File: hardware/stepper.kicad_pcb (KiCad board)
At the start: 4 copper layers, 40 x 40 mm, 128 parts, among them J101 USB-MINI-B-SMD, J102 DRILL, J103 DRILL, J104 DRILL, J105 DRILL, J401 STACK-UP-HIGH, J402 STACK-DOWN, J403 STACK-UP-HIGH, J404 STACK-DOWN, P201 black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

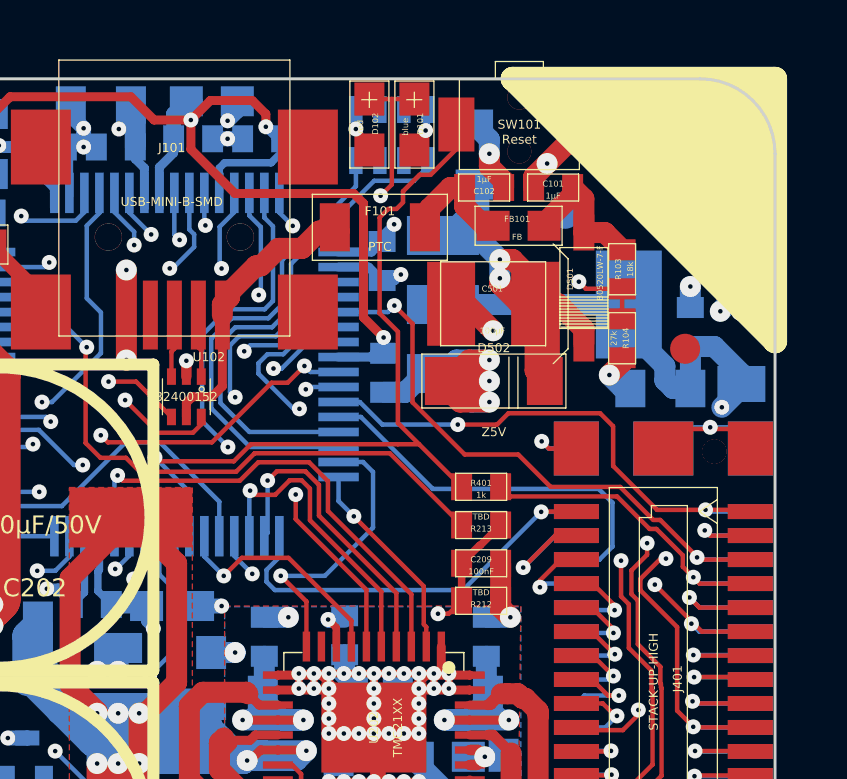
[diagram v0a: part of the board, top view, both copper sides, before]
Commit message: update to new library settings
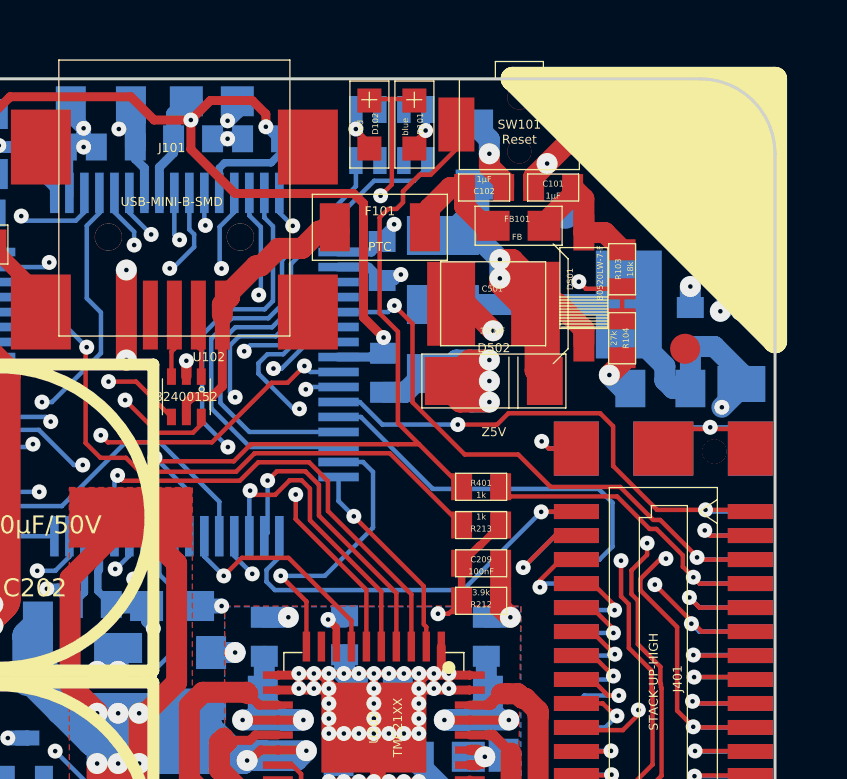
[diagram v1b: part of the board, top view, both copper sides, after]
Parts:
- C103, C104: value 9pF -> DNP
- D101, D102: footprint kicad-libraries:D0603E -> kicad-libraries:D0603
- R212: value TBD -> 3.9k
- R213: value TBD -> 1k
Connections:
- FILTER301 pad 8: (no net) -> Net-(FILTER301-Pad8)
- FILTER301 pad 9: (no net) -> Net-(FILTER301-Pad9)
- FILTER302 pad 8: (no net) -> Net-(FILTER302-Pad8)
- FILTER302 pad 9: (no net) -> Net-(FILTER302-Pad9)
- J101 pad 4: (no net) -> Net-(J101-Pad4)
- RP101 pad 2: (no net) -> Net-(RP101-Pad2)
- RP101 pad 3: (no net) -> Net-(RP101-Pad3)
- RP101 pad 6: (no net) -> Net-(RP101-Pad6)
- RP101 pad 7: (no net) -> Net-(RP101-Pad7)
- RP301 pad 6: (no net) -> Net-(RP301-Pad6)
- RP301 pad 7: (no net) -> Net-(RP301-Pad7)
- U101 pad 40: (no net) -> Net-(U101-Pad40)
- U101 pad 50: (no net) -> Net-(U101-Pad50)
- U202 pad 9: (no net) -> Net-(U202-Pad9)
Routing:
- net VSTACK: track 86.5 -> 88.1 mm
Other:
- board text added: "Copyright Tinkerforge GmbH 2016. This documentation describes Open Hardware and is licensed under the CERN OHL v. 1.1. You may redistribute and modify this documentation under the terms of the CERN OHL v.1.1. (http://ohwr.org/cernohl). This documentation is distributed WITHOUT ANY EXPRESS OR IMPLIED WARRANTY, INCLUDING OF MERCHANTABILITY, SATISFACTORY QUALITY AND FITNESS FOR A PARTICULAR PURPOSE.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"
- board text removed: "Copyright Tinkerforge GmbH 2015. This documentation describes Open Hardware and is licensed under the CERN OHL v. 1.1. You may redistribute and modify this documentation under the terms of the CERN OHL v.1.1. (http://ohwr.org/cernohl). This documentation is distributed WITHOUT ANY EXPRESS OR IMPLIED WARRANTY, INCLUDING OF MERCHANTABILITY, SATISFACTORY QUALITY AND FITNESS FOR A PARTICULAR PURPOSE.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"

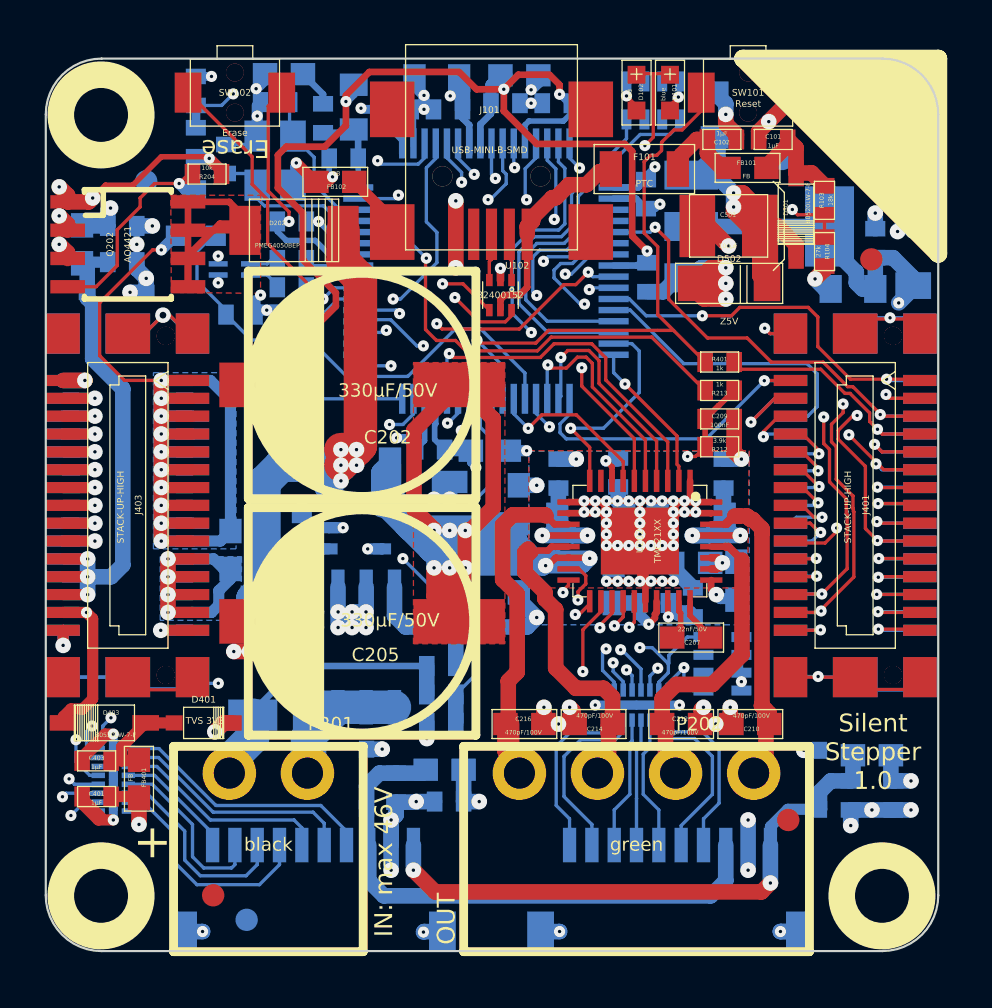
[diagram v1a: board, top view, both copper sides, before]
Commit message: fix tf logo, remove current measurement
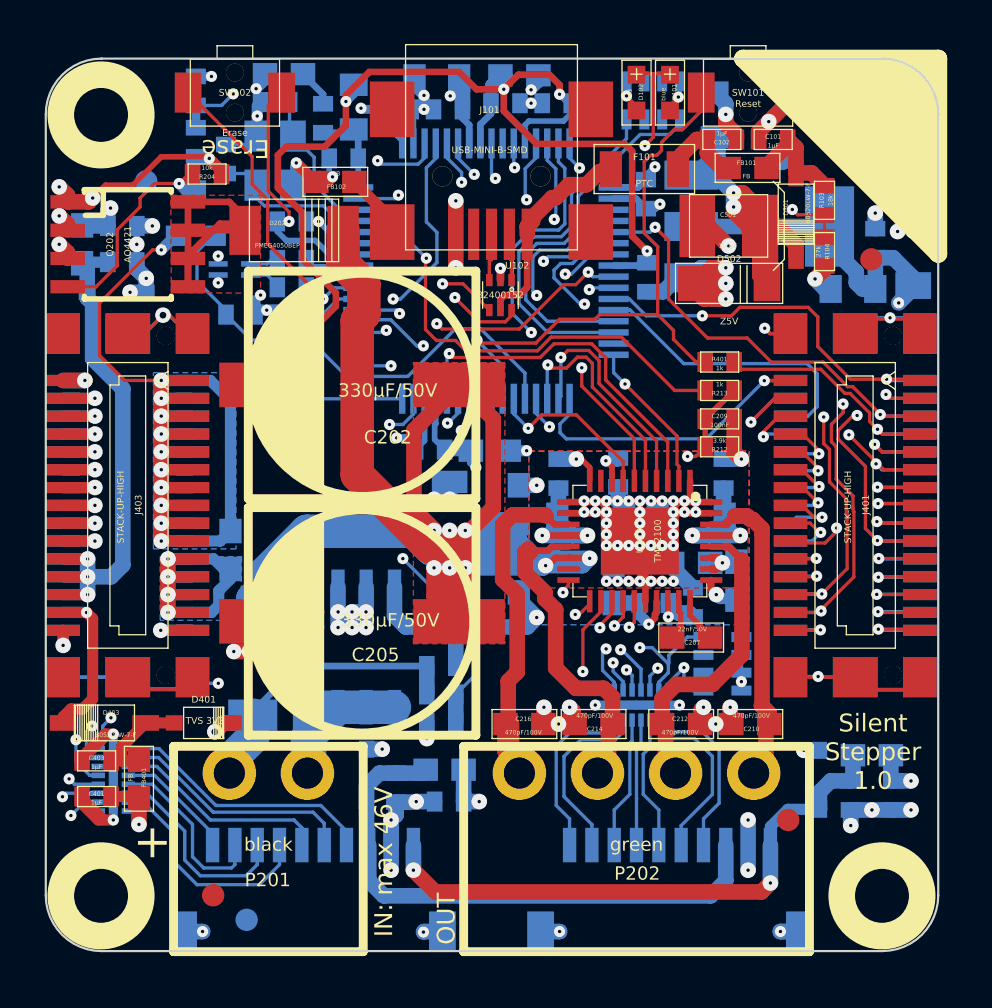
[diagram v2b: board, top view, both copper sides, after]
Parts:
- removed the G*** at (157.5, 85.2)
- removed R209: 0.01, kicad-libraries:1206
- removed R210: 10k, kicad-libraries:0402E
- removed U201: ZXCT1086, kicad-libraries:SOT23-5
- added G***: Logo_31x31, kicad-libraries:Logo_31x31, B.Cu at (157.5, 85.2)
- U202: value TMC21XX -> TMC2100
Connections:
- net PWR-CS_CFG3 renamed PWR-CFG3
- net PWR-DCEN_CFG4 renamed PWR-CFG4
- net PWR-DCIN_CFG5 renamed PWR-CFG5
- net PWR-SCK_CFG2 renamed PWR-CFG2
- net PWR-SD0_CFG0 renamed PWR-CFG0
- net PWR-SDI_CFG1 renamed PWR-CFG1
- D202 pad 2: Net-(D202-Pad2) -> VEE
- D203 pad 2: Net-(D202-Pad2) -> VEE
- U101 pad 10: PWR-CUR-SENSE -> Net-(U101-Pad10)
- U101 pad 31: PWR-SPI_MODE -> Net-(U101-Pad31)
- U101 pad 41: PWR-DC0 -> Net-(U101-Pad41)
- U202 pad 10: PWR-SPI_MODE -> STACK-PGND
- U202 pad 17: PWR-DC0 -> Net-(U202-Pad17)
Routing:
- net Net-(D202-Pad2): track 30.2 -> 0.00 mm, vias 5 -> 0
- net 3V3: track 192.1 -> 169.6 mm, vias 14 -> 13
- net PWR-CUR-SENSE: track 21.5 -> 0.00 mm, vias 2 -> 0
- net VEE: track 77.8 -> 95.8 mm
- net PWR-DC0: track 14.6 -> 0.00 mm, vias 2 -> 0
- net PWR-SPI_MODE: track 9.60 -> 0.00 mm, vias 1 -> 0
- net GND: track 435.4 -> 430.1 mm, vias 63 -> 62
- net STACK-PGND: track 217.1 -> 218.5 mm
- net Net-(R210-Pad2): track 1.28 -> 0.00 mm

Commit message: fix wrong bricklet select voltages
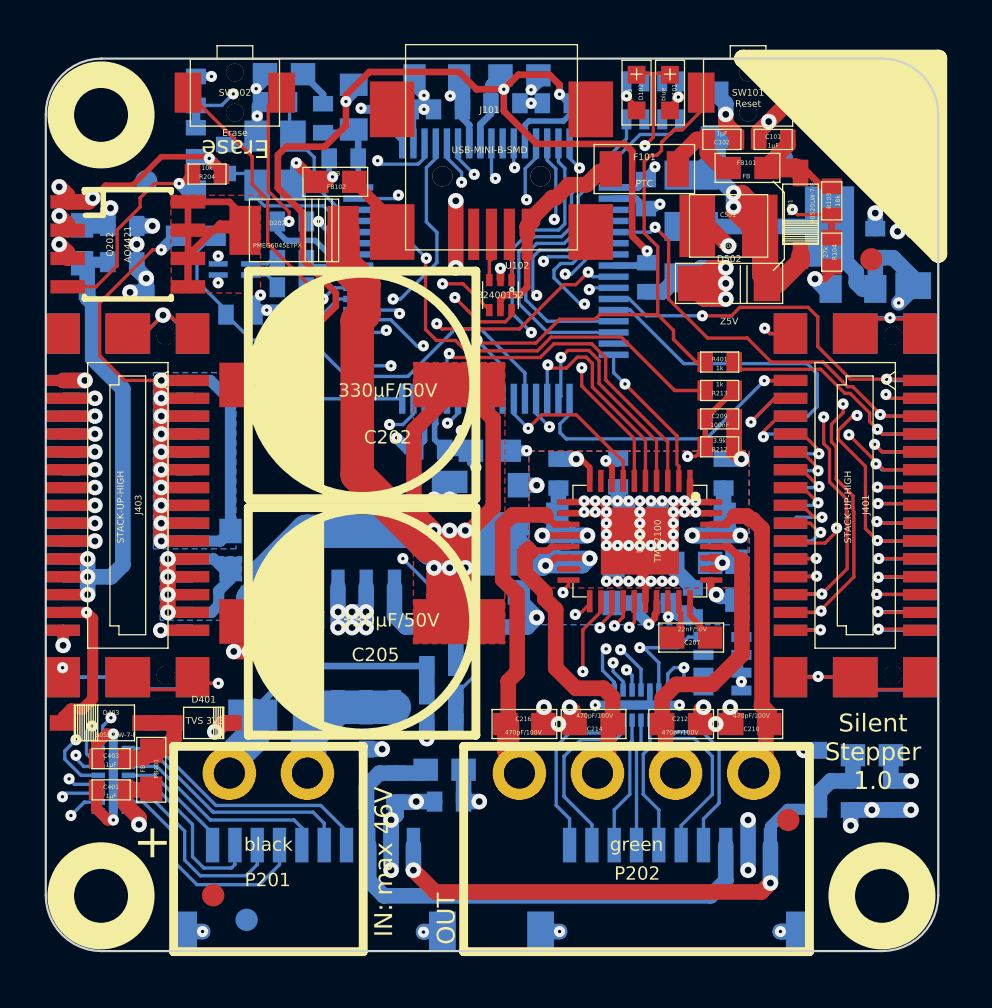
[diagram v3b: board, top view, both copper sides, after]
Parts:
- D202, D203: value PMEG4050BEP -> PMEG6045ETPX
- Q201: value FDS8449 -> AO4438
- moved C401 0.72 mm to (129.7, 105.5)
- moved FB401 0.68 mm to (131.4, 104.7)
- moved C403 0.66 mm to (129.7, 104.2)
- moved R103 0.33 mm to (161.9, 79.2)
- moved R104 0.33 mm to (161.9, 81.5)
- moved D501 0.20 mm to (160.6, 79.8)
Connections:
- FILTER301 pad 14: GND -> 3V3
- FILTER302 pad 14: 3V3 -> GND
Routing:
- net 3V3: track 169.6 -> 177.6 mm
- net GND: track 430.1 -> 428.7 mm, vias 62 -> 63
- net BRICKLET-IO0_3: track 39.4 -> 40.0 mm
- net BRICKLET-I2C-SCL: track 54.7 -> 55.3 mm

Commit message: detail routing improvements
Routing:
- net STACK-RESET: track 26.7 -> 28.3 mm
- net STACK-I2C-SDA/JTAG-TDI: track 14.4 -> 12.9 mm
- net STACK-I2C-SCL/JTAG-TDO: track 23.3 -> 24.4 mm
- net Net-(J401-Pad6): track 2.99 -> 3.74 mm
- net STACK-PGND: track 218.5 -> 219.2 mm
- net Net-(J401-Pad8): track 3.04 -> 3.73 mm
- net 3V3: track 177.6 -> 178.2 mm
- net Net-(SW102-Pad1): track 13.6 -> 14.1 mm
- net PWR-CFG5: track 24.6 -> 25.1 mm
- added copper zone on F.Cu, net STACK-PVCC

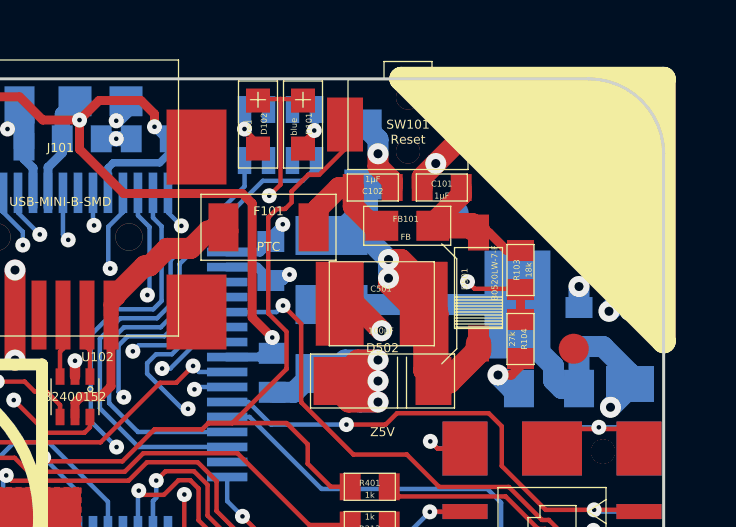
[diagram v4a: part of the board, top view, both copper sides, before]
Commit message: move leds from border, delete to near doku
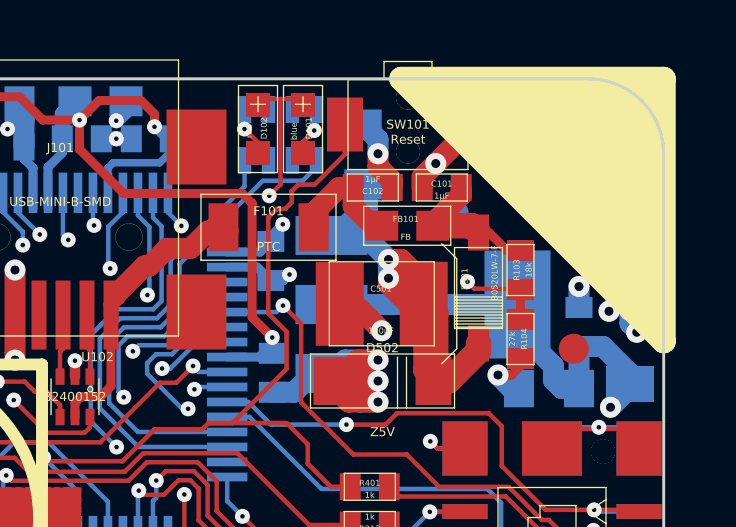
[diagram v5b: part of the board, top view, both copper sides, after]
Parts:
- moved D101 0.15 mm to (154.7, 74.5)
- moved D102 0.15 mm to (153.2, 74.5)
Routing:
- net GND: track 428.7 -> 429.5 mm
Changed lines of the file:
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@@
     (links 407)
     (no_connects 2)
-    (area 126.671069 72.726549 166.772591 112.825531)
+    (area 125.845139 71.945139 283.420502 165.440043)
     (thickness 1.6002)
     (drawings 63)
-    (tracks 2561)
+    (tracks 2563)
     (zones 0)
     (modules 125)
@@
   )
   (layers
-    (0 Vorderseite signal hide)
+    (0 Vorderseite signal)
     (1 GND signal hide)
     (2 VCC signal hide)
@@
     (34 B.Paste user)
     (35 F.Paste user)
-    (36 B.SilkS user)
-    (37 F.SilkS user)
+    (36 B.SilkS user hide)
+    (37 F.SilkS user hide)
     (38 B.Mask user)
     (39 F.Mask user)
@@
   )
   (setup
-    (last_trace_width 0.1524)
+    (last_trace_width 0.70104)
     (user_trace_width 0.1524)
     (user_trace_width 0.25)
@@
     (aux_axis_origin 126.72568 112.776)
     (grid_origin 166.15 99.35)
-    (visible_elements FFFE9FFF)
+    (visible_elements FFFEDFFF)
     (pcbplotparams
-      (layerselection 0x00010_00000000)
+      (layerselection 0x010fc_80000007)
       (usegerberextensions true)
       (excludeedgelayer true)
@@
   )
   (module kicad-libraries:D0603 (layer Vorderseite)
-    (at 154.7 74.3 270)
+    (at 154.7 74.45 270)
     (attr smd)
     (fp_text reference D101 (at -0.025 -0.2 270) (layer F.SilkS)
@@
   )
   (module kicad-libraries:D0603 (layer Vorderseite)
-    (at 153.2 74.3 270)
+    (at 153.2 74.45 270)
     (attr smd)
     (fp_text reference D102 (at -0.025 -0.2 270) (layer F.SilkS)
@@
   (segment (start 151.7767 99.1722) (end 146.4141 99.1722) (width 0.1498) (layer VCC) (net 11))
   (segment (start 151.837 99.2325) (end 151.7767 99.1722) (width 0.1498) (layer VCC) (net 11))
+  (segment (start 165.6 79.55074) (end 165.6 80.925) (width 0.70104) (layer Rückseite) (net 12))
+  (via (at 165.825 81.225) (size 0.7) (drill 0.3) (layers Vorderseite Rückseite) (net 12))
+  (segment (start 165.825 81.15) (end 165.825 81.225) (width 0.70104) (layer Rückseite) (net 12))
+  (segment (start 165.6 80.925) (end 165.825 81.15) (width 0.70104) (layer Rückseite) (net 12))
   (segment (start 134.4562 100.7754) (end 133.57734 100.7754) (width 0.1524) (layer Vorderseite) (net 12))
   (segment (start 133.57734 100.7754) (end 133.30068 100.49874) (width 0.1524) (layer Vorderseite) (net 12))
@@
   (via (at 157.2 82.15) (size 0.7) (drill 0.3) (layers Vorderseite Rückseite) (net 12))
   (via (at 157.2 82.85) (size 0.7) (drill 0.3) (layers Vorderseite Rückseite) (net 12))
-  (via (at 166.3 80.5) (size 0.7) (drill 0.3) (layers Vorderseite Rückseite) (net 12))
   (via (at 165.6 80.5) (size 0.7) (drill 0.3) (layers Vorderseite Rückseite) (net 12))
   (via (at 163.9 79.7) (size 0.7) (drill 0.3) (layers Vorderseite Rückseite) (net 12))
@@
   (segment (start 155.651 82.85) (end 155.651 82.9757) (width 0.701) (layer Vorderseite) (net 12))
   (segment (start 155.651 82.85) (end 155.825 82.85) (width 0.701) (layer Vorderseite) (net 12))
-  (segment (start 165.6 79.8) (end 166.3 80.5) (width 0.701) (layer Rückseite) (net 12))
   (segment (start 165.6 79.5507) (end 165.6 79.8) (width 0.701) (layer Rückseite) (net 12))
   (segment (start 165.6 79.5507) (end 165.6 79.825) (width 0.701) (layer Rückseite) (net 12))
@@
   (segment (start 155.625 86.375) (end 154.8577 85.6077) (width 0.1524) (layer Vorderseite) (net 26))
   (segment (start 154.3216 76.8966) (end 154.3216 76.5284) (width 0.1524) (layer Vorderseite) (net 26))
-  (segment (start 154.875 75.975) (end 155.2432 75.975) (width 0.1524) (layer Vorderseite) (net 26))
-  (segment (start 154.3216 76.5284) (end 154.875 75.975) (width 0.1524) (layer Vorderseite) (net 26))
+  (segment (start 154.55 76.3) (end 155.0932 76.3) (width 0.1524) (layer Vorderseite) (net 26))
+  (segment (start 154.3216 76.5284) (end 154.55 76.3) (width 0.1524) (layer Vorderseite) (net 26))
   (segment (start 153.5422 80.5954) (end 154.1515 81.2047) (width 0.1498) (layer Vorderseite) (net 26))
   (segment (start 153.5422 77.402) (end 153.5422 80.5954) (width 0.1498) (layer Vorderseite) (net 26))
   (segment (start 153.83 77.1142) (end 153.5422 77.402) (width 0.1498) (layer Vorderseite) (net 26))
   (segment (start 154.104 77.1142) (end 153.83 77.1142) (width 0.1498) (layer Vorderseite) (net 26))
-  (segment (start 156.101 75.1172) (end 155.2432 75.975) (width 0.1498) (layer Vorderseite) (net 26))
+  (segment (start 156.101 75.2922) (end 155.0932 76.3) (width 0.1498) (layer Vorderseite) (net 26))
   (segment (start 154.3216 76.8966) (end 154.104 77.1142) (width 0.1498) (layer Vorderseite) (net 26))
   (segment (start 154.1515 84.2515) (end 154.8577 84.9577) (width 0.1524) (layer Vorderseite) (net 26))
@@
   (segment (start 147.1993 88.0226) (end 147.1993 86.5443) (width 0.1498) (layer Rückseite) (net 26))
   (segment (start 147.1993 86.5443) (end 146.0534 85.3984) (width 0.1498) (layer Rückseite) (net 26))
-  (segment (start 156.101 74.3) (end 156.101 75.1172) (width 0.1498) (layer Vorderseite) (net 26))
+  (segment (start 156.101 74.3) (end 156.101 75.2922) (width 0.1498) (layer Vorderseite) (net 26))
   (via (at 161.5892 88.8388) (size 0.5) (layers Vorderseite Rückseite) (net 27))
   (via (at 147.7348 77.6629) (size 0.5) (layers Vorderseite Rückseite) (net 27))
